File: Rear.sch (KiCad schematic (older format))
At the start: 39 parts, among them J11 FAN, J2 USB, J3 12V 300mA, J6 COM, Q1 IRLML6402, U3 FT230XS, U5 AP3211

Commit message: Rewrite references
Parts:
- renumbered C18 to C14, C13 to C15, C15 to C16, C16 to C17, C17 to C18, C14 to C19, C9 to C20, C23 to C21, C24 to C23, C10 to C24, DZ2 to DZ1, DZ1 to DZ2, J3 to J10, J6 to J8, J2 to J9, MP2 to MP10, MP3 to MP11, MP1 to MP9, R10 to R27, R11 to R28, R38 to R29, R37 to R30, R8 to R31, R9 to R32, R12 to R33, R2 to R34, R6 to R35, R7 to R36, R24 to R37, R39 to R38, U3 to U4

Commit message: More finalization
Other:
- note added: "810mV"
- note added: "Breakaway PCB - install at rear of unit"
- note added: "Layout note: grounded screw near DC-DC"
- moved on the sheet: C14, C15, C16, C20, C24, DZ2, J10, J8, J9, MP10, MP11, MP9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

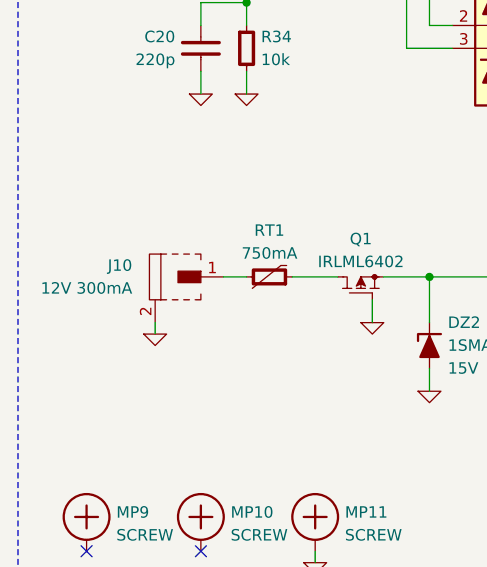
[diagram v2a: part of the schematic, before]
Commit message: Update BOM references
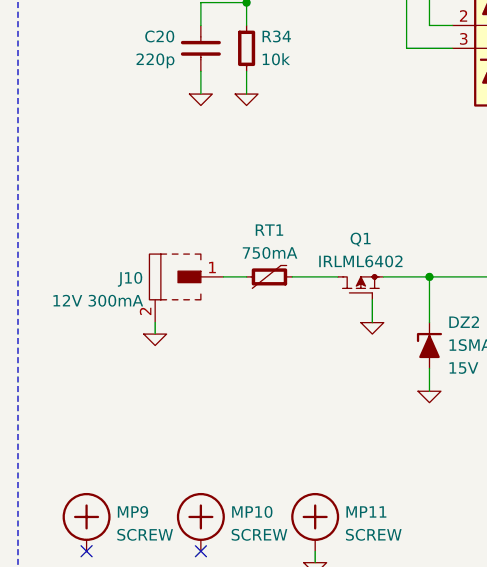
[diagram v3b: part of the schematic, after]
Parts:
- Q1: BOM SEMI IRF IRLML6402 -> PMOS IRF IRLML6402
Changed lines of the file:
@@
 U 1 1 563D6C64
 P 1500 5200
-F 0 "J10" H 1700 5250 50  0000 L CNN
-F 1 "12V 300mA" H 1700 5150 50  0000 L CNN
+F 0 "J10" H 1652 5194 50  0000 L CNN
+F 1 "12V 300mA" H 1652 5094 50  0000 L CNN
 F 2 "conn-cui:CONN-PJ-037A" H 1500 5200 50  0001 C CNN
 F 3 "" H 1600 5200 60  0000 C CNN
@@
 F 2 "smd-semi:SOT-23" H 2300 5100 60  0001 C CNN
 F 3 "" H 2600 5300 60  0000 C CNN
-F 4 "SEMI IRF IRLML6402" H 2300 5000 60  0001 C CNN "BOM"
+F 4 "PMOS IRF IRLML6402" H 2300 5000 60  0001 C CNN "BOM"
 	1    2300 5250
 	0    1    -1   0
